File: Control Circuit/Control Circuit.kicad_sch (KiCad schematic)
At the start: 3 parts, among them U1 Adafruit DPS310, U2 STM32F411CEU6

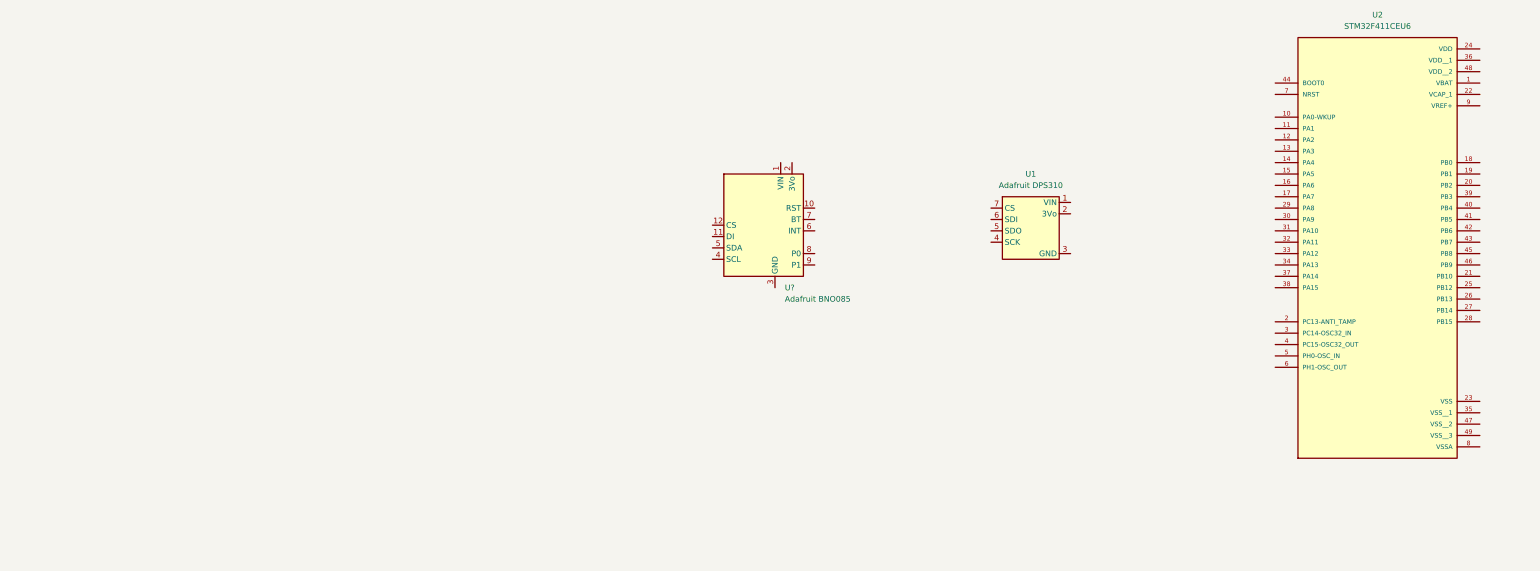
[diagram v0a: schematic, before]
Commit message: added stm32f405 board files
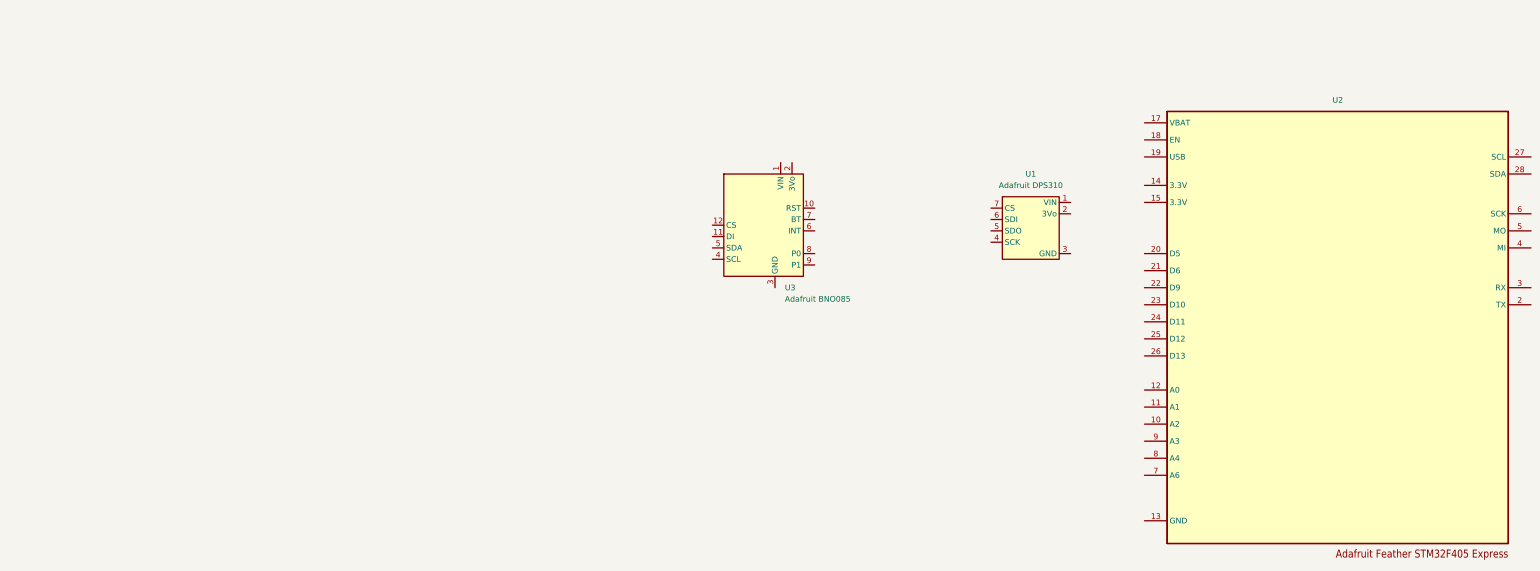
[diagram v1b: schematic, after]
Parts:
- removed U2: STM32F411CEU6, STM32F411CEU6:QFN50P700X700X60-49N, symbol Stm32F411:STM32F411CEU6
- added U2: ~, STM32F405:Adafruit Feather STM32F405 Express, symbol Adafruit STM32F405:Adafruit_express_STM32F405
- U3: renamed from U?; now in the parts list
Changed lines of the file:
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@@
+    )
+  )
+  (symbol (lib_id "Adafruit STM32F405:Adafruit_express_STM32F405") (at 341.63 92.71 0) (unit 1)
+    (in_bom yes) (on_board yes) (dnp no) (fields_autoplaced)
+    (property "Reference" "U2" (at 341.63 44.45 0)
+      (effects (font (size 1.27 1.27)))
+    )
+    (property "Value" "~" (at 341.63 92.71 0)
+      (effects (font (size 1.27 1.27)))
+    )
+    (property "Footprint" "STM32F405:Adafruit Feather STM32F405 Express" (at 341.63 92.71 0)
+      (effects (font (size 1.27 1.27)) hide)
+    )
+    (property "Datasheet" "" (at 341.63 92.71 0)
+      (effects (font (size 1.27 1.27)) hide)
+    )
+    (pin "15")
+    (pin "18")
+    (pin "23")
+    (pin "9")
+    (pin "25")
+    (pin "5")
+    (pin "28")
+    (pin "8")
+    (pin "3")
+    (pin "11")
+    (pin "20")
+    (pin "17")
+    (pin "19")
+    (pin "22")
+    (pin "14")
+    (pin "24")
+    (pin "6")
+    (pin "13")
+    (pin "2")
+    (pin "12")
+    (pin "4")
+    (pin "7")
+    (pin "27")
+    (pin "26")
+    (pin "10")
+    (pin "21")
+    (instances
+      (project "Control Circuit"
+        (path "/c22302ef-9dbe-40df-968a-d3109ceb2872"
+          (reference "U2") (unit 1)
+        )
+      )
     )
   )
   (symbol (lib_id "Adafruit BNO085:Adafruit_BNO085") (at 215.9 67.31 0) (unit 1)
-    (in_bom no) (on_board no) (dnp no) (fields_autoplaced)
-    (property "Reference" "U?" (at 218.0941 86.36 0)
+    (in_bom yes) (on_board yes) (dnp no) (fields_autoplaced)
+    (property "Reference" "U3" (at 218.0941 86.36 0)
       (effects (font (size 1.27 1.27)) (justify left))
     )
@@
       (project "Control Circuit"
         (path "/c22302ef-9dbe-40df-968a-d3109ceb2872"
-          (reference "U?") (unit 1)
+          (reference "U3") (unit 1)
         )
       )
-    )
-  )
-  (symbol (lib_id "Stm32F411:STM32F411CEU6") (at 350.52 73.66 0) (unit 1)
-    (in_bom yes) (on_board yes) (dnp no) (fields_autoplaced)
-    (property "Reference" "U2" (at 350.52 25.4 0)
-      (effects (font (size 1.27 1.27)))
-    )
-    (property "Value" "STM32F411CEU6" (at 350.52 27.94 0)
-      (effects (font (size 1.27 1.27)))
-    )
-    (property "Footprint" "STM32F411CEU6:QFN50P700X700X60-49N" (at 350.52 73.66 0)
-      (effects (font (size 1.27 1.27)) (justify bottom) hide)
-    )
-    (property "Datasheet" "" (at 350.52 73.66 0)
-      (effects (font (size 1.27 1.27)) hide)
-    )
-    (property "MF" "STMicroelectronics" (at 350.52 73.66 0)
-      (effects (font (size 1.27 1.27)) (justify bottom) hide)
-    )
-    (property "MAXIMUM_PACKAGE_HEIGHT" "0.65mm" (at 350.52 73.66 0)
-      (effects (font (size 1.27 1.27)) (justify bottom) hide)
-    )
-    (property "Package" "UFQFN-48 STMicroelectronics" (at 350.52 73.66 0)
-      (effects (font (size 1.27 1.27)) (justify bottom) hide)
-    )
-    (property "Price" "None" (at 350.52 73.66 0)
-      (effects (font (size 1.27 1.27)) (justify bottom) hide)
-    )
-    (property "Check_prices" "https://www.snapeda.com/parts/STM32F411CEU6/STMicroelectronics/view-part/?ref=eda" (at 350.52 73.66 0)
-      (effects (font (size 1.27 1.27)) (justify bottom) hide)
-    )
-    (property "STANDARD" "IPC-7351B" (at 350.52 73.66 0)
-      (effects (font (size 1.27 1.27)) (justify bottom) hide)
-    )
-    (property "PARTREV" "7" (at 350.52 73.66 0)
-      (effects (font (size 1.27 1.27)) (justify bottom) hide)
-    )
-    (property "SnapEDA_Link" "https://www.snapeda.com/parts/STM32F411CEU6/STMicroelectronics/view-part/?ref=snap" (at 350.52 73.66 0)
-      (effects (font (size 1.27 1.27)) (justify bottom) hide)
-    )
-    (property "MP" "STM32F411CEU6" (at 350.52 73.66 0)
-      (effects (font (size 1.27 1.27)) (justify bottom) hide)
-    )
-    (property "Purchase-URL" "https://www.snapeda.com/api/url_track_click_mouser/?unipart_id=383021&manufacturer=STMicroelectronics&part_name=STM32F411CEU6&search_term=stm32f411" (at 350.52 73.66 0)
-      (effects (font (size 1.27 1.27)) (justify bottom) hide)
-    )
-    (property "Description" "\nARM® Cortex®-M4 STM32F4 Microcontroller IC 32-Bit Single-Core 100MHz 512KB (512K x 8) FLASH 48-UFQFPN (7x7)\n" (at 350.52 73.66 0)
-      (effects (font (size 1.27 1.27)) (justify bottom) hide)
-    )
-    (property "Availability" "In Stock" (at 350.52 73.66 0)
-      (effects (font (size 1.27 1.27)) (justify bottom) hide)
-    )
-    (property "MANUFACTURER" "STMicroelectronics" (at 350.52 73.66 0)
-      (effects (font (size 1.27 1.27)) (justify bottom) hide)
-    )
-    (pin "43")
-    (pin "2")
-    (pin "37")
-    (pin "22")
-    (pin "45")
-    (pin "44")
-    (pin "13")
-    (pin "5")
-    (pin "9")
-    (pin "46")
-    (pin "39")
-    (pin "10")
-    (pin "17")
-    (pin "23")
-    (pin "26")
-    (pin "19")
-    (pin "30")
-    (pin "27")
-    (pin "42")
-    (pin "8")
-    (pin "41")
-    (pin "14")
-    (pin "21")
-    (pin "3")
-    (pin "33")
-    (pin "12")
-    (pin "15")
-    (pin "24")
-    (pin "48")
-    (pin "11")
-    (pin "31")
-    (pin "34")
-    (pin "40")
-    (pin "7")
-    (pin "18")
-    (pin "29")
-    (pin "4")
-    (pin "47")
-    (pin "6")
-    (pin "35")
-    (pin "28")
-    (pin "36")
-    (pin "25")
-    (pin "49")
-    (pin "1")
-    (pin "16")
-    (pin "32")
-    (pin "38")
-    (pin "20")
-    (instances
-      (project "Control Circuit"
-        (path "/c22302ef-9dbe-40df-968a-d3109ceb2872"
-          (reference "U2") (unit 1)
-        )
-      )

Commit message: fixed .step file not loading
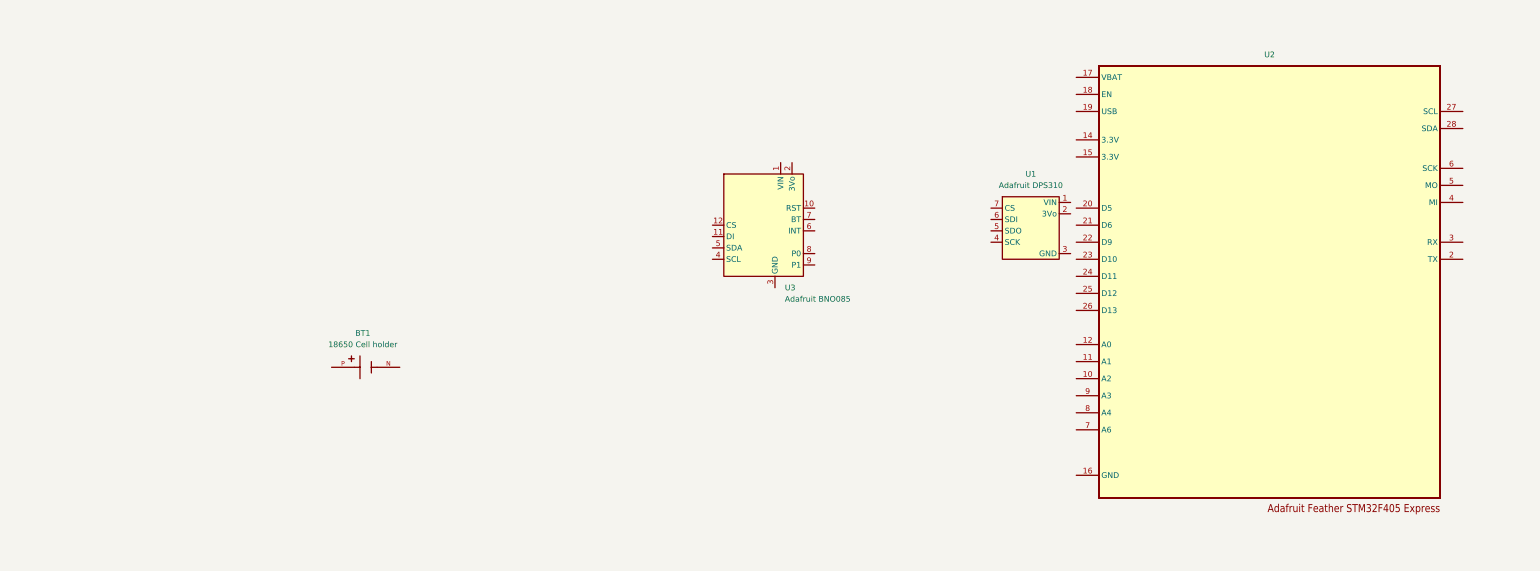
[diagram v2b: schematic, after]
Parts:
- added BT1: 18650 Cell holder, 18650 Cell Holder:18560 holder, symbol 18650 Cell holder:18650 Cell holder
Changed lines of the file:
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@@
-    )
-  )
-  (symbol (lib_id "Adafruit STM32F405:Adafruit_express_STM32F405") (at 341.63 92.71 0) (unit 1)
-    (in_bom yes) (on_board yes) (dnp no) (fields_autoplaced)
-    (property "Reference" "U2" (at 341.63 44.45 0)
-      (effects (font (size 1.27 1.27)))
-    )
-    (property "Value" "~" (at 341.63 92.71 0)
-      (effects (font (size 1.27 1.27)))
-    )
-    (property "Footprint" "STM32F405:Adafruit Feather STM32F405 Express" (at 341.63 92.71 0)
-      (effects (font (size 1.27 1.27)) hide)
-    )
-    (property "Datasheet" "" (at 341.63 92.71 0)
-      (effects (font (size 1.27 1.27)) hide)
-    )
-    (pin "15")
-    (pin "18")
-    (pin "23")
-    (pin "9")
-    (pin "25")
-    (pin "5")
-    (pin "28")
-    (pin "8")
-    (pin "3")
-    (pin "11")
-    (pin "20")
-    (pin "17")
-    (pin "19")
-    (pin "22")
-    (pin "14")
-    (pin "24")
-    (pin "6")
-    (pin "13")
-    (pin "2")
-    (pin "12")
-    (pin "4")
-    (pin "7")
-    (pin "27")
-    (pin "26")
-    (pin "10")
-    (pin "21")
-    (instances
-      (project "Control Circuit"
-        (path "/c22302ef-9dbe-40df-968a-d3109ceb2872"
-          (reference "U2") (unit 1)
-        )
-      )
     )
   )
@@
         )
       )
+    )
+  )
+  (symbol (lib_id "Adafruit STM32F405:Adafruit_express_STM32F405") (at 326.39 82.55 0) (unit 1)
+    (in_bom yes) (on_board yes) (dnp no) (fields_autoplaced)
+    (property "Reference" "U2" (at 326.39 34.29 0)
+      (effects (font (size 1.27 1.27)))
+    )
+    (property "Value" "~" (at 326.39 82.55 0)
+      (effects (font (size 1.27 1.27)))
+    )
+    (property "Footprint" "STM32F405:Adafruit Feather STM32F405 Express" (at 326.39 82.55 0)
+      (effects (font (size 1.27 1.27)) hide)
+    )
+    (property "Datasheet" "" (at 326.39 82.55 0)
+      (effects (font (size 1.27 1.27)) hide)
+    )
+    (pin "20")
+    (pin "5")
+    (pin "18")
+    (pin "26")
+    (pin "8")
+    (pin "2")
+    (pin "17")
+    (pin "16")
+    (pin "11")
+    (pin "15")
+    (pin "27")
+    (pin "21")
+    (pin "7")
+    (pin "10")
+    (pin "9")
+    (pin "25")
+    (pin "22")
+    (pin "28")
+    (pin "4")
+    (pin "23")
+    (pin "3")
+    (pin "14")
+    (pin "24")
+    (pin "12")
+    (pin "6")
+    (pin "19")
+    (instances
+      (project "Control Circuit"
+        (path "/c22302ef-9dbe-40df-968a-d3109ceb2872"
+          (reference "U2") (unit 1)
+        )
+      )
+    )
+  )
+  (symbol (lib_id "18650 Cell holder:18650 Cell holder") (at 124.46 104.14 0) (unit 1)
+    (in_bom yes) (on_board yes) (dnp no) (fields_autoplaced)
+    (property "Reference" "BT1" (at 123.825 96.52 0)
+      (effects (font (size 1.27 1.27)))
+    )
+    (property "Value" "18650 Cell holder" (at 123.825 99.06 0)
+      (effects (font (size 1.27 1.27)))
+    )
+    (property "Footprint" "18650 Cell Holder:18560 holder" (at 124.46 104.14 0)
+      (effects (font (size 1.27 1.27)) (justify bottom) hide)
+    )
+    (property "Datasheet" "" (at 124.46 104.14 0)
+      (effects (font (size 1.27 1.27)) hide)
+    )
+    (property "MF" "" (at 124.46 104.14 0)
+      (effects (font (size 1.27 1.27)) (justify bottom) hide)
+    )
+    (property "MAXIMUM_PACKAGE_HEIGHT" "" (at 124.46 104.14 0)
+      (effects (font (size 1.27 1.27)) (justify bottom) hide)
+    )
+    (property "Package" "" (at 124.46 104.14 0)
+      (effects (font (size 1.27 1.27)) (justify bottom) hide)
+    )
+    (property "Price" "" (at 124.46 104.14 0)
+      (effects (font (size 1.27 1.27)) (justify bottom) hide)
+    )
+    (property "Check_prices" "" (at 124.46 104.14 0)
+      (effects (font (size 1.27 1.27)) (justify bottom) hide)
+    )
+    (property "STANDARD" "" (at 124.46 104.14 0)
+      (effects (font (size 1.27 1.27)) (justify bottom) hide)
+    )
+    (property "PARTREV" "" (at 124.46 104.14 0)
+      (effects (font (size 1.27 1.27)) (justify bottom) hide)
+    )
+    (property "SnapEDA_Link" "" (at 124.46 104.14 0)
+      (effects (font (size 1.27 1.27)) (justify bottom) hide)
+    )
+    (property "MP" "" (at 124.46 104.14 0)
+      (effects (font (size 1.27 1.27)) (justify bottom) hide)
+    )
+    (property "Purchase-URL" "" (at 124.46 104.14 0)
+      (effects (font (size 1.27 1.27)) (justify bottom) hide)
+    )
+    (property "Description" "\nSMT Holder for 18650 Battery\n" (at 102.87 102.87 0) (do_not_autoplace)
+      (effects (font (size 1.27 1.27)) (justify bottom) hide)
+    )
+    (property "SNAPEDA_PN" "" (at 124.46 104.14 0)
+      (effects (font (size 1.27 1.27)) (justify bottom) hide)
+    )
+    (property "Availability" "" (at 124.46 104.14 0)
+      (effects (font (size 1.27 1.27)) (justify bottom) hide)
+    )
+    (property "MANUFACTURER" "" (at 124.46 104.14 0)
+      (effects (font (size 1.27 1.27)) (justify bottom) hide)
+    )
+    (pin "N")
+    (pin "P")
+    (instances
+      (project "Control Circuit"
+        (path "/c22302ef-9dbe-40df-968a-d3109ceb2872"
+          (reference "BT1") (unit 1)
+        )
+      )

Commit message: added symbol and foot print for boost converter
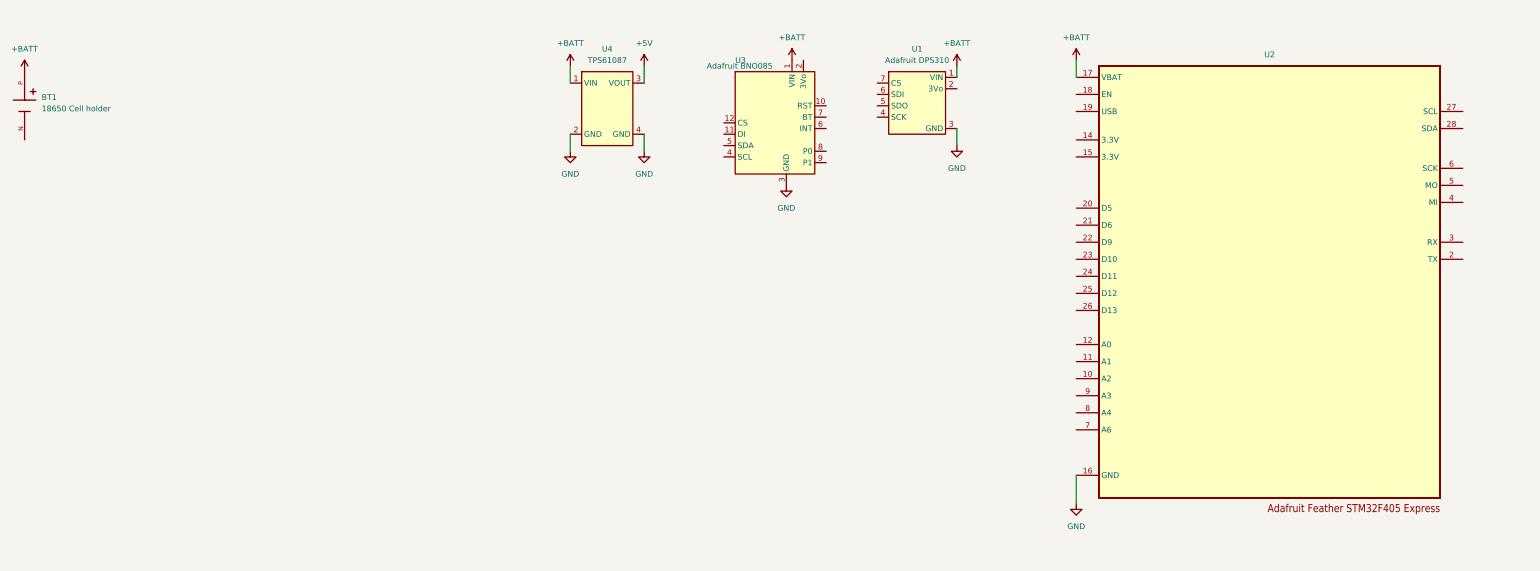
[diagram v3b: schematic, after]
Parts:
- added U4: TPS61087, Boost Converter:TPS61087 Breakout, symbol Boost Converter:Boost_Converter
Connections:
- net +BATT: now reaches U1.1 (VIN)
- net +BATT: now also BT1.P, U2.17 (VBAT), U3.1 (VIN), U4.1 (VIN)
- net GND: now reaches U1.3 (GND)
- net GND: now also U2.16 (GND), U3.3 (GND), U4.2 (GND), U4.4 (GND)
- new net +5V: U4.3 (VOUT)
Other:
- moved on the sheet: BT1, U1, U3
